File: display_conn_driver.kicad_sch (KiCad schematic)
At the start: 9 parts, among them IC5 AW9364DNR

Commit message: Minor changes to styling
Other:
- note added: "Display Connector"
- note added: "Display Driver"
- moved on the sheet: C29, IC5

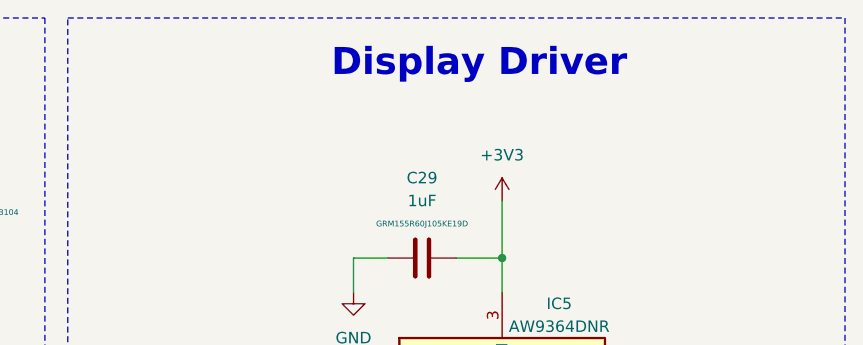
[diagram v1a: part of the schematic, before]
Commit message: Промяна по оформление и текст в схемата
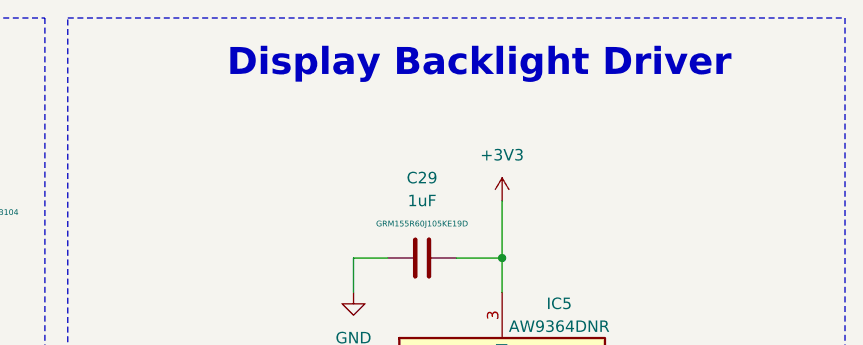
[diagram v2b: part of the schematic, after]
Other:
- note added: "Display Backlight Driver"
- note removed: "Display Driver"
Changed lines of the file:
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@@
 		)
 	)
-	(text "Display Driver"
+	(text "Display Backlight Driver"
 		(exclude_from_sim no)
 		(at 154.94 19.05 0)
